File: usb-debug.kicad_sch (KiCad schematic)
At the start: 87 parts, among them IC1 NCP380LSNAJAAT1G, IC15 TPS7A0518PDBVT, IC3 NCP380LSNAJAAT1G, IC7 HD3SS3220, J11 632723300011, T6 BSS138APW, T7 BSS138APW, T9 BSS138APW, U8 74LVC1G07GV

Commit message: ADD U8 to the local library
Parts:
- removed U8: 74LVC1G07GV, antmicro-footprints:SOT-753, symbol antmicroLogicBuffersDriversReceiversTransceivers:74LVC1G07GV
- added U8: 74LVC1G07GV, jetson-nano-baseboard-footprints:SOT-753, symbol jetson-nano-baseboard:74LVC1G07GV
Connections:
- net 5V0_SYS: now also U8.5 (VCC)
- net GND: now also U8.3 (GND)
- net OTG_USB_ID: now also U8.2 (A)
- net ~{OTG_USB_ID_DET}: now also U8.4 (Y)
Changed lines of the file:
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@@
     (pin "2")
-  )
-  (symbol (lib_id "antmicroLogicBuffersDriversReceiversTransceivers:74LVC1G07GV") (at 122.555 202.565 0) (mirror y) (unit 1)
-    (in_bom yes) (on_board yes)
-    (property "Reference" "U8" (id 0) (at 125.73 194.945 0)
-      (effects (font (size 1.524 1.524)))
-    )
-    (property "Value" "74LVC1G07GV" (id 1) (at 131.445 210.82 0)
-      (effects (font (size 1.524 1.524)))
-    )
-    (property "Footprint" "antmicro-footprints:SOT-753" (id 2) (at 117.475 198.755 0)
-      (effects (font (size 1.524 1.524)) (justify left) hide)
-    )
-    (property "Datasheet" "http://www.ti.com/general/docs/suppproductinfo.tsp?distId=10&gotoUrl=http%3A%2F%2Fwww.ti.com%2Flit%2Fgpn%2Fsn74lvc1g07" (id 3) (at 117.475 196.215 0)
-      (effects (font (size 1.524 1.524)) (justify left) hide)
-    )
-    (property "MPN" "74LVC1G07GV,125" (id 4) (at 118.745 193.675 0)
-      (effects (font (size 1.524 1.524)) (justify left) hide)
-    )
-    (property "Manufacturer" "Texas Instruments" (id 5) (at 118.745 191.135 0)
-      (effects (font (size 1.524 1.524)) (justify left) hide)
-    )
-    (pin "1")
-    (pin "2")
-    (pin "3")
-    (pin "4")
-    (pin "5")
   )
   (symbol (lib_id "jetson-nano-baseboard:NCP380LSNAJAAT1G") (at 278.765 38.1 0) (unit 1)
@@
     (pin "2")
   )
+  (symbol (lib_id "jetson-nano-baseboard:74LVC1G07GV") (at 122.555 202.565 0) (mirror y) (unit 1)
+    (in_bom yes) (on_board yes)
+    (property "Reference" "U8" (id 0) (at 125.095 194.945 0)
+      (effects (font (size 1.524 1.524)))
+    )
+    (property "Value" "74LVC1G07GV" (id 1) (at 130.81 210.82 0)
+      (effects (font (size 1.524 1.524)))
+    )
+    (property "Footprint" "jetson-nano-baseboard-footprints:SOT-753" (id 2) (at 117.475 198.755 0)
+      (effects (font (size 1.524 1.524)) (justify left) hide)
+    )
+    (property "Datasheet" "http://www.ti.com/general/docs/suppproductinfo.tsp?distId=10&gotoUrl=http%3A%2F%2Fwww.ti.com%2Flit%2Fgpn%2Fsn74lvc1g07" (id 3) (at 117.475 196.215 0)
+      (effects (font (size 1.524 1.524)) (justify left) hide)
+    )
+    (property "MPN" "74LVC1G07GV,125" (id 4) (at 118.745 193.675 0)
+      (effects (font (size 1.524 1.524)) (justify left) hide)
+    )
+    (property "Manufacturer" "Texas Instruments" (id 5) (at 118.745 191.135 0)
+      (effects (font (size 1.524 1.524)) (justify left) hide)
+    )
+    (pin "1")
+    (pin "2")
+    (pin "3")
+    (pin "4")
+    (pin "5")
+  )
   (symbol (lib_id "jetson-nano-baseboard:GND") (at 134.62 191.77 0) (unit 1)

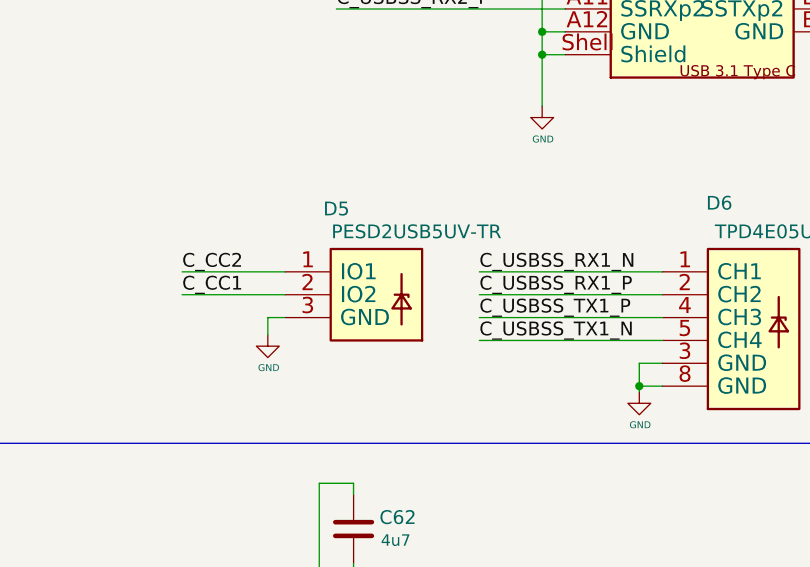
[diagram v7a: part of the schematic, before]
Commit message: Replace D5 and D10 with a copy of D12
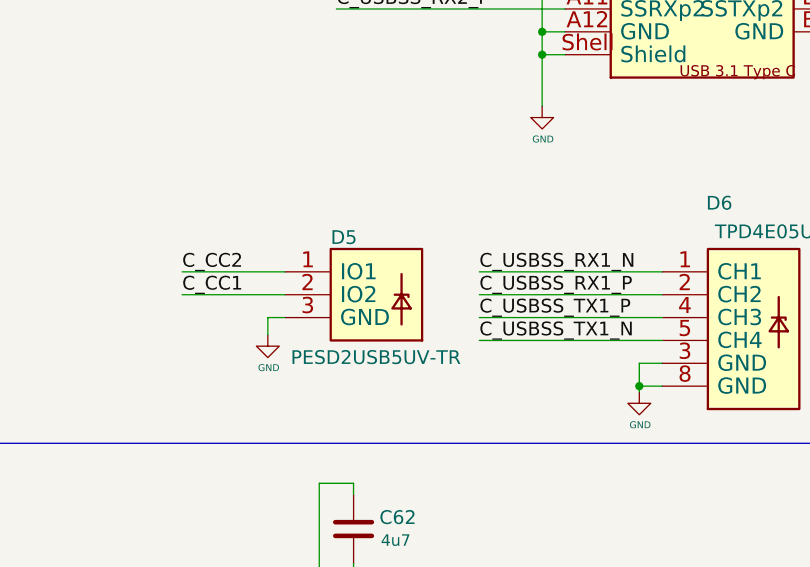
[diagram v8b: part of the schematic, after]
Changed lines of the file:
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@@
     (pin "2")
-  )
-  (symbol (lib_id "jetson-nano-baseboard:PESD2USB5UV-TR") (at 299.085 139.7 0) (unit 1)
-    (in_bom yes) (on_board yes)
-    (property "Reference" "D5" (id 0) (at 299.72 132.715 0)
-      (effects (font (size 1.524 1.524)))
-    )
-    (property "Value" "PESD2USB5UV-TR" (id 1) (at 308.61 135.255 0)
-      (effects (font (size 1.524 1.524)))
-    )
-    (property "Footprint" "jetson-nano-baseboard-footprints:SOT-23s" (id 2) (at 300.355 134.62 0)
-      (effects (font (size 1.524 1.524)) hide)
-    )
-    (property "Datasheet" "https://assets.nexperia.com/documents/data-sheet/PESD2USB5UV-T.pdf" (id 3) (at 299.085 139.7 0)
-      (effects (font (size 1.524 1.524)) hide)
-    )
-    (property "MPN" "PESD2USB5UV-TR " (id 4) (at 291.465 132.08 0)
-      (effects (font (size 1.27 1.27)) hide)
-    )
-    (property "Manufacturer" "Nexperia " (id 5) (at 291.465 129.54 0)
-      (effects (font (size 1.27 1.27)) hide)
-    )
-    (pin "1")
-    (pin "2")
-    (pin "3")
   )
   (symbol (lib_id "jetson-nano-baseboard:PESD2USB5UV-TR") (at 370.84 239.395 270) (unit 1)
@@
     (pin "2")
   )
+  (symbol (lib_id "jetson-nano-baseboard:PESD2USB5UV-TR") (at 299.085 139.7 0) (unit 1)
+    (in_bom yes) (on_board yes)
+    (property "Reference" "D5" (id 0) (at 299.085 135.89 0)
+      (effects (font (size 1.524 1.524)) (justify left))
+    )
+    (property "Value" "PESD2USB5UV-TR" (id 1) (at 294.64 149.225 0)
+      (effects (font (size 1.524 1.524)) (justify left))
+    )
+    (property "Footprint" "jetson-nano-baseboard-footprints:SOT-23s" (id 2) (at 300.355 134.62 0)
+      (effects (font (size 1.524 1.524)) hide)
+    )
+    (property "Datasheet" "https://assets.nexperia.com/documents/data-sheet/PESD2USB5UV-T.pdf" (id 3) (at 299.085 139.7 0)
+      (effects (font (size 1.524 1.524)) hide)
+    )
+    (property "MPN" "PESD2USB5UV-TR " (id 4) (at 291.465 132.08 0)
+      (effects (font (size 1.27 1.27)) hide)
+    )
+    (property "Manufacturer" "Nexperia " (id 5) (at 291.465 129.54 0)
+      (effects (font (size 1.27 1.27)) hide)
+    )
+    (pin "1")
+    (pin "2")
+    (pin "3")
+  )
   (symbol (lib_id "jetson-nano-baseboard:NCP380LSNAJAAT1G") (at 278.765 38.1 0) (unit 1)
